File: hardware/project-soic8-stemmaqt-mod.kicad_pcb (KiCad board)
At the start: 2 copper layers, 15.5 x 8.4 mm, 2 parts, among them J1 SM04B-SRSS-TB(LF)(SN), U1 24LC00

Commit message: Add version
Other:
- board text added: "François Gervais 9 mai 2021 v1.0"
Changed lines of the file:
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@@
   (general
     (thickness 0.1016)
-    (drawings 17)
+    (drawings 18)
     (tracks 29)
     (zones 0)
@@
     )
   )
+  (gr_text "François Gervais\n9 mai 2021\nv1.0" (at 36.25 20.45) (layer B.SilkS)
+    (effects (font (size 0.6 0.6) (thickness 0.1)) (justify left mirror))
+  )
   (gr_arc (start 27.85 20.6) (end 28 20.6) (angle -90) (layer Edge.Cuts) (width 0.05))

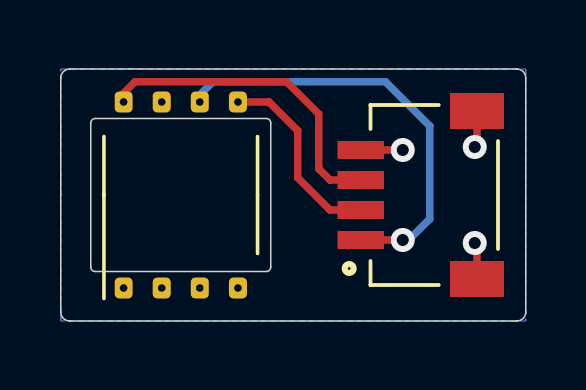
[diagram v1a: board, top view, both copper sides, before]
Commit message: Match Stemma QT pinout
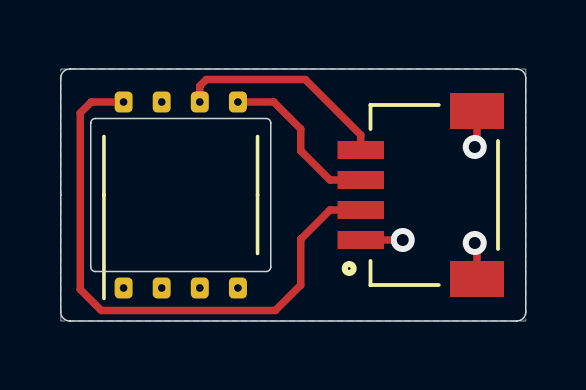
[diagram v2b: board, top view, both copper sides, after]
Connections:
- J1 pad 1: /SCL -> GND
- J1 pad 2: /SDA -> VCC
- J1 pad 3: VCC -> /SDA
- J1 pad 4: GND -> /SCL
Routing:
- net VCC: track 10.8 -> 19.4 mm
- net /SCL: track 14.4 -> 7.26 mm, vias 1 -> 0
- net /SDA: track 6.51 -> 5.60 mm
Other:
- board text added: "François Gervais v"
- board text removed: "François Gervais 9 mai 2021 v1.0"

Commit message: Add version
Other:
- board text added: "François Gervais 28 mai 2021 v1.0-3-gf25257a"
- board text removed: "François Gervais v"
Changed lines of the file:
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@@
       (effects (font (size 1 1) (thickness 0.15)))
     )
+    (fp_line (start 3.7 -2.7) (end -3.7 -2.7) (layer F.CrtYd) (width 0.05))
+    (fp_line (start 3.7 2.7) (end 3.7 -2.7) (layer F.CrtYd) (width 0.05))
+    (fp_line (start -3.7 2.7) (end 3.7 2.7) (layer F.CrtYd) (width 0.05))
+    (fp_line (start -3.7 -2.7) (end -3.7 2.7) (layer F.CrtYd) (width 0.05))
+    (fp_line (start -1.95 -1.475) (end -0.975 -2.45) (layer F.Fab) (width 0.1))
+    (fp_line (start -1.95 2.45) (end -1.95 -1.475) (layer F.Fab) (width 0.1))
+    (fp_line (start 1.95 2.45) (end -1.95 2.45) (layer F.Fab) (width 0.1))
+    (fp_line (start 1.95 -2.45) (end 1.95 2.45) (layer F.Fab) (width 0.1))
+    (fp_line (start -0.975 -2.45) (end 1.95 -2.45) (layer F.Fab) (width 0.1))
+    (fp_line (start 0 -2.56) (end -3.45 -2.56) (layer F.SilkS) (width 0.12))
+    (fp_line (start 0 -2.56) (end 1.95 -2.56) (layer F.SilkS) (width 0.12))
+    (fp_line (start 0 2.56) (end -1.95 2.56) (layer F.SilkS) (width 0.12))
     (fp_line (start 0 2.56) (end 1.95 2.56) (layer F.SilkS) (width 0.12))
-    (fp_line (start 0 2.56) (end -1.95 2.56) (layer F.SilkS) (width 0.12))
-    (fp_line (start 0 -2.56) (end 1.95 -2.56) (layer F.SilkS) (width 0.12))
-    (fp_line (start 0 -2.56) (end -3.45 -2.56) (layer F.SilkS) (width 0.12))
-    (fp_line (start -0.975 -2.45) (end 1.95 -2.45) (layer F.Fab) (width 0.1))
-    (fp_line (start 1.95 -2.45) (end 1.95 2.45) (layer F.Fab) (width 0.1))
-    (fp_line (start 1.95 2.45) (end -1.95 2.45) (layer F.Fab) (width 0.1))
-    (fp_line (start -1.95 2.45) (end -1.95 -1.475) (layer F.Fab) (width 0.1))
-    (fp_line (start -1.95 -1.475) (end -0.975 -2.45) (layer F.Fab) (width 0.1))
-    (fp_line (start -3.7 -2.7) (end -3.7 2.7) (layer F.CrtYd) (width 0.05))
-    (fp_line (start -3.7 2.7) (end 3.7 2.7) (layer F.CrtYd) (width 0.05))
-    (fp_line (start 3.7 2.7) (end 3.7 -2.7) (layer F.CrtYd) (width 0.05))
-    (fp_line (start 3.7 -2.7) (end -3.7 -2.7) (layer F.CrtYd) (width 0.05))
     (fp_text user %R (at 0 0 90) (layer F.Fab)
       (effects (font (size 0.98 0.98) (thickness 0.15)))
@@
       (effects (font (size 1.000567 1.000567) (thickness 0.015)))
     )
+    (fp_line (start -3.65 5.025) (end -3.65 -1.025) (layer F.CrtYd) (width 0.05))
+    (fp_line (start 3.65 5.025) (end -3.65 5.025) (layer F.CrtYd) (width 0.05))
+    (fp_line (start 3.65 -1.025) (end 3.65 5.025) (layer F.CrtYd) (width 0.05))
+    (fp_line (start -3.65 -1.025) (end 3.65 -1.025) (layer F.CrtYd) (width 0.05))
+    (fp_circle (center -2.45 -0.385) (end -2.35 -0.385) (layer F.Fab) (width 0.3))
+    (fp_line (start -1.8 4.575) (end 1.8 4.575) (layer F.SilkS) (width 0.127))
+    (fp_line (start 3 0.325) (end 3 2.6) (layer F.SilkS) (width 0.127))
+    (fp_line (start 2.2 0.325) (end 3 0.325) (layer F.SilkS) (width 0.127))
+    (fp_line (start -3 0.325) (end -3 2.6) (layer F.SilkS) (width 0.127))
+    (fp_line (start -2.2 0.325) (end -3 0.325) (layer F.SilkS) (width 0.127))
+    (fp_line (start -3 4.575) (end -3 0.325) (layer F.Fab) (width 0.127))
+    (fp_line (start 3 4.575) (end -3 4.575) (layer F.Fab) (width 0.127))
+    (fp_line (start 3 0.325) (end 3 4.575) (layer F.Fab) (width 0.127))
+    (fp_line (start -3 0.325) (end 3 0.325) (layer F.Fab) (width 0.127))
     (fp_circle (center -2.45 -0.385) (end -2.35 -0.385) (layer F.SilkS) (width 0.3))
-    (fp_line (start -3 0.325) (end 3 0.325) (layer F.Fab) (width 0.127))
-    (fp_line (start 3 0.325) (end 3 4.575) (layer F.Fab) (width 0.127))
-    (fp_line (start 3 4.575) (end -3 4.575) (layer F.Fab) (width 0.127))
-    (fp_line (start -3 4.575) (end -3 0.325) (layer F.Fab) (width 0.127))
-    (fp_line (start -2.2 0.325) (end -3 0.325) (layer F.SilkS) (width 0.127))
-    (fp_line (start -3 0.325) (end -3 2.6) (layer F.SilkS) (width 0.127))
-    (fp_line (start 2.2 0.325) (end 3 0.325) (layer F.SilkS) (width 0.127))
-    (fp_line (start 3 0.325) (end 3 2.6) (layer F.SilkS) (width 0.127))
-    (fp_line (start -1.8 4.575) (end 1.8 4.575) (layer F.SilkS) (width 0.127))
-    (fp_circle (center -2.45 -0.385) (end -2.35 -0.385) (layer F.Fab) (width 0.3))
-    (fp_line (start -3.65 -1.025) (end 3.65 -1.025) (layer F.CrtYd) (width 0.05))
-    (fp_line (start 3.65 -1.025) (end 3.65 5.025) (layer F.CrtYd) (width 0.05))
-    (fp_line (start 3.65 5.025) (end -3.65 5.025) (layer F.CrtYd) (width 0.05))
-    (fp_line (start -3.65 5.025) (end -3.65 -1.025) (layer F.CrtYd) (width 0.05))
     (pad S2 smd rect (at 2.8 3.875 90) (size 1.2 1.8) (layers F.Cu F.Paste F.Mask)
       (net 1 GND))
@@
     )
   )
-  (gr_text "François Gervais\n\nv" (at 36.25 20.45) (layer B.SilkS)
+  (gr_text "François Gervais\n28 mai 2021\nv1.0-3-gf25257a" (at 36.4 20.4) (layer B.SilkS)
     (effects (font (size 0.6 0.6) (thickness 0.1)) (justify left mirror))
   )

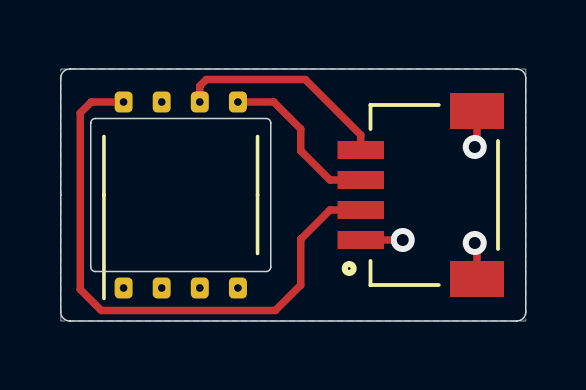
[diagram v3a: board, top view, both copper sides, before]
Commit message: New pcb with castellated holes
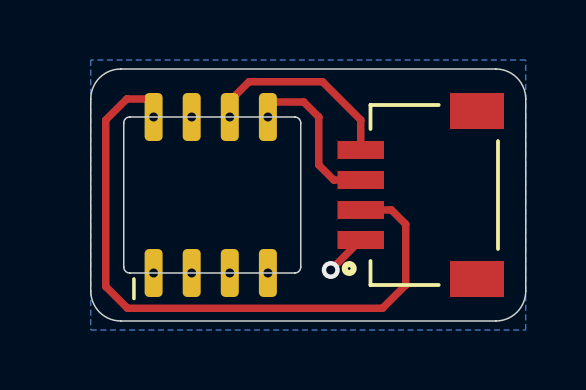
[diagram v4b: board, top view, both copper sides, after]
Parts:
- moved U1 1.00 mm to (26.0, 23.0)
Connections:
- U1 pad 1: Net-(U1-Pad1) -> unconnected-(U1-A0-Pad1)
- U1 pad 2: Net-(U1-Pad2) -> unconnected-(U1-A1-Pad2)
- U1 pad 3: Net-(U1-Pad3) -> unconnected-(U1-A2-Pad3)
- U1 pad 7: Net-(U1-Pad7) -> unconnected-(U1-WP-Pad7)
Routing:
- net VCC: track 19.4 -> 22.3 mm
- net GND: track 3.86 -> 1.41 mm, vias 3 -> 1
- net /SCL: track 7.26 -> 6.69 mm
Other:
- board size 15.5 x 8.4 mm -> 14.5 x 8.4 mm
- net class Default removed
- board text added: "v1.0-3 -gf25257a"
- board text removed: "François Gervais 28 mai 2021 v1.0-3-gf25257a"

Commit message: Add VCC pour
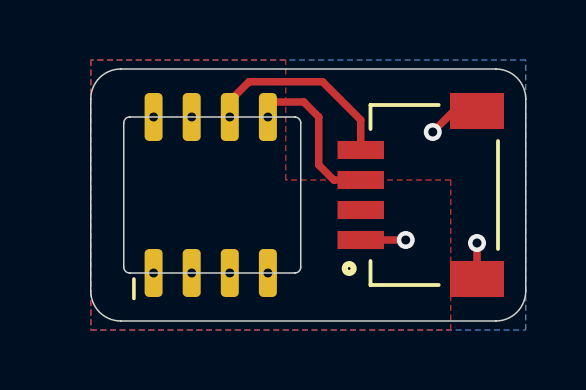
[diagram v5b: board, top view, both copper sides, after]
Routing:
- net VCC: track 22.3 -> 0.00 mm
- net GND: track 1.41 -> 4.46 mm, vias 1 -> 3
- added copper zone on F.Cu, net VCC
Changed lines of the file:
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@@
 	(segment
 		(start 31 24.5)
-		(end 30 25.5)
+		(end 32.5 24.5)
+		(width 0.25)
+		(layer "F.Cu")
+		(net 1)
+	)
+	(segment
+		(start 34.875 24.6)
+		(end 34.875 25.8)
+		(width 0.25)
+		(layer "F.Cu")
+		(net 1)
+	)
+	(segment
+		(start 34.875 20.2)
+		(end 34.1 20.2)
+		(width 0.25)
+		(layer "F.Cu")
+		(net 1)
+	)
+	(segment
+		(start 34.1 20.2)
+		(end 33.4 20.9)
 		(width 0.25)
 		(layer "F.Cu")
@@
 	)
 	(via
-		(at 30 25.5)
+		(at 33.4 20.9)
 		(size 0.6)
 		(drill 0.3)
@@
 		(net 1)
 	)
-	(segment
-		(start 24.095 19.995)
-		(end 23.9 19.8)
-		(width 0.25)
-		(layer "F.Cu")
-		(net 2)
+	(via
+		(at 32.5 24.5)
+		(size 0.6)
+		(drill 0.3)
+		(layers "F.Cu" "B.Cu")
+		(net 1)
 	)
-	(segment
-		(start 32.5 26)
-		(end 32.5 23.975)
-		(width 0.25)
-		(layer "F.Cu")
-		(net 2)
-	)
-	(segment
-		(start 22.5 20.5)
-		(end 22.5 26.05)
-		(width 0.25)
-		(layer "F.Cu")
-		(net 2)
-	)
-	(segment
-		(start 23.2 19.8)
-		(end 22.5 20.5)
-		(width 0.25)
-		(layer "F.Cu")
-		(net 2)
-	)
-	(segment
-		(start 22.5 26.05)
-		(end 23.225 26.775)
-		(width 0.25)
-		(layer "F.Cu")
-		(net 2)
-	)
-	(segment
-		(start 32.025 23.5)
-		(end 31 23.5)
-		(width 0.25)
-		(layer "F.Cu")
-		(net 2)
-	)
-	(segment
-		(start 32.5 23.975)
-		(end 32.025 23.5)
-		(width 0.25)
-		(layer "F.Cu")
-		(net 2)
-	)
-	(segment
-		(start 23.9 19.8)
-		(end 23.2 19.8)
-		(width 0.25)
-		(layer "F.Cu")
-		(net 2)
-	)
-	(segment
-		(start 24.095 20.4)
-		(end 24.095 19.995)
-		(width 0.25)
-		(layer "F.Cu")
-		(net 2)
-	)
-	(segment
-		(start 23.225 26.775)
-		(end 31.725 26.775)
-		(width 0.25)
-		(layer "F.Cu")
-		(net 2)
-	)
-	(segment
-		(start 31.725 26.775)
-		(end 32.5 26)
-		(width 0.25)
-		(layer "F.Cu")
-		(net 2)
+	(via
+		(at 34.875 24.6)
+		(size 0.6)
+		(drill 0.3)
+		(layers "F.Cu" "B.Cu")
+		(net 1)
 	)
 	(segment
@@
 	)
 	(zone
+		(net 2)
+		(net_name "VCC")
+		(layer "F.Cu")
+		(hatch edge 0.5)
+		(priority 1)
+		(connect_pads yes
+			(clearance 0.2)
+		)
+		(min_thickness 0.25)
+		(filled_areas_thickness no)
+		(fill yes
+			(thermal_gap 0.5)
+			(thermal_bridge_width 0.5)
+			(smoothing fillet)
+			(radius 1)
+		)
+		(polygon
+			(pts
+				(xy 28.5 22.5) (xy 28.5 18.5) (xy 22 18.5) (xy 22 27.5) (xy 34 27.5) (xy 34 22.5)
+			)
+		)
+	)
+	(zone
